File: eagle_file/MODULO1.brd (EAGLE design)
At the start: 160 x 100 mm, 6 parts, among them IC1 MCP23017SP

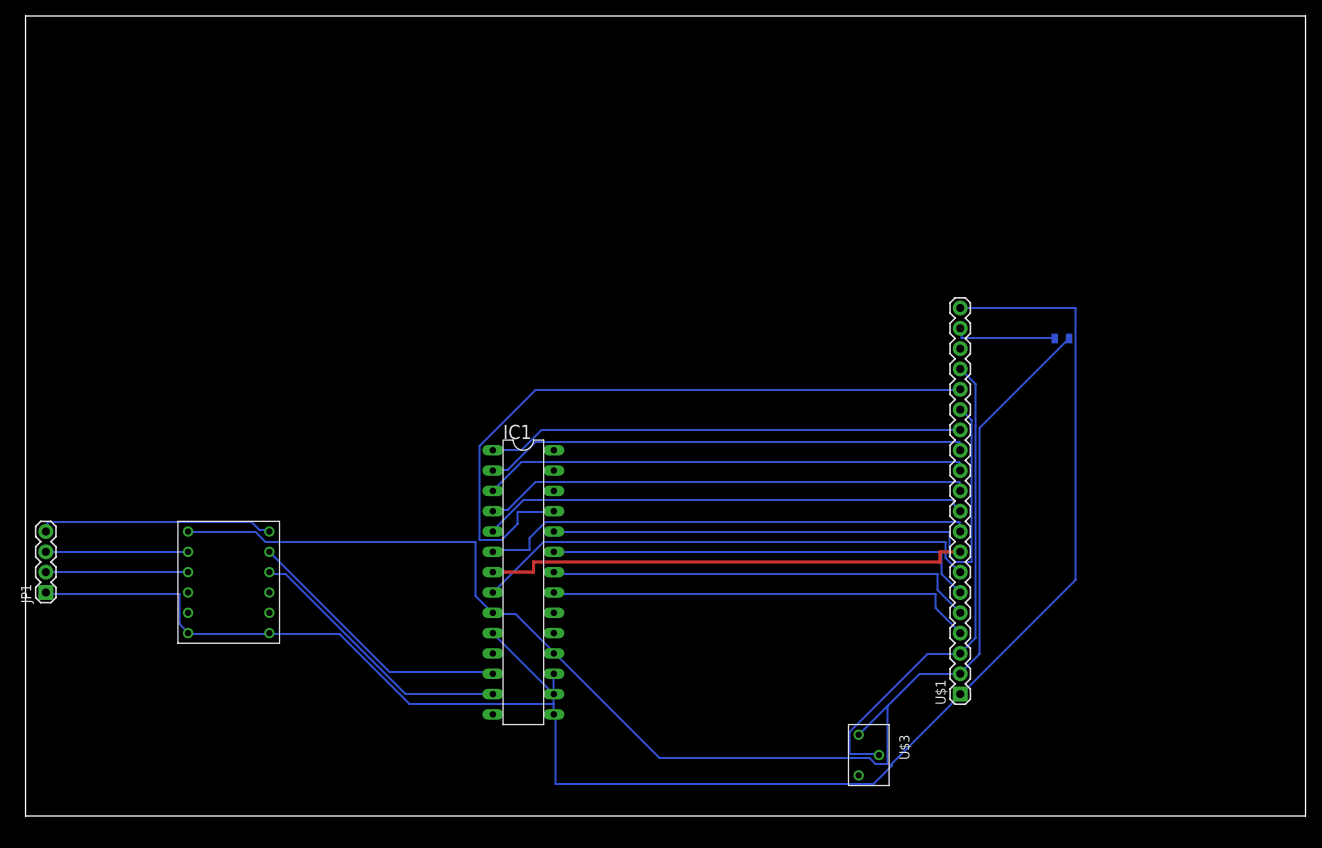
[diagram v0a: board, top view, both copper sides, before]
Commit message: Modulo 0 pdf
Modulo 0 senza contorno ai fori
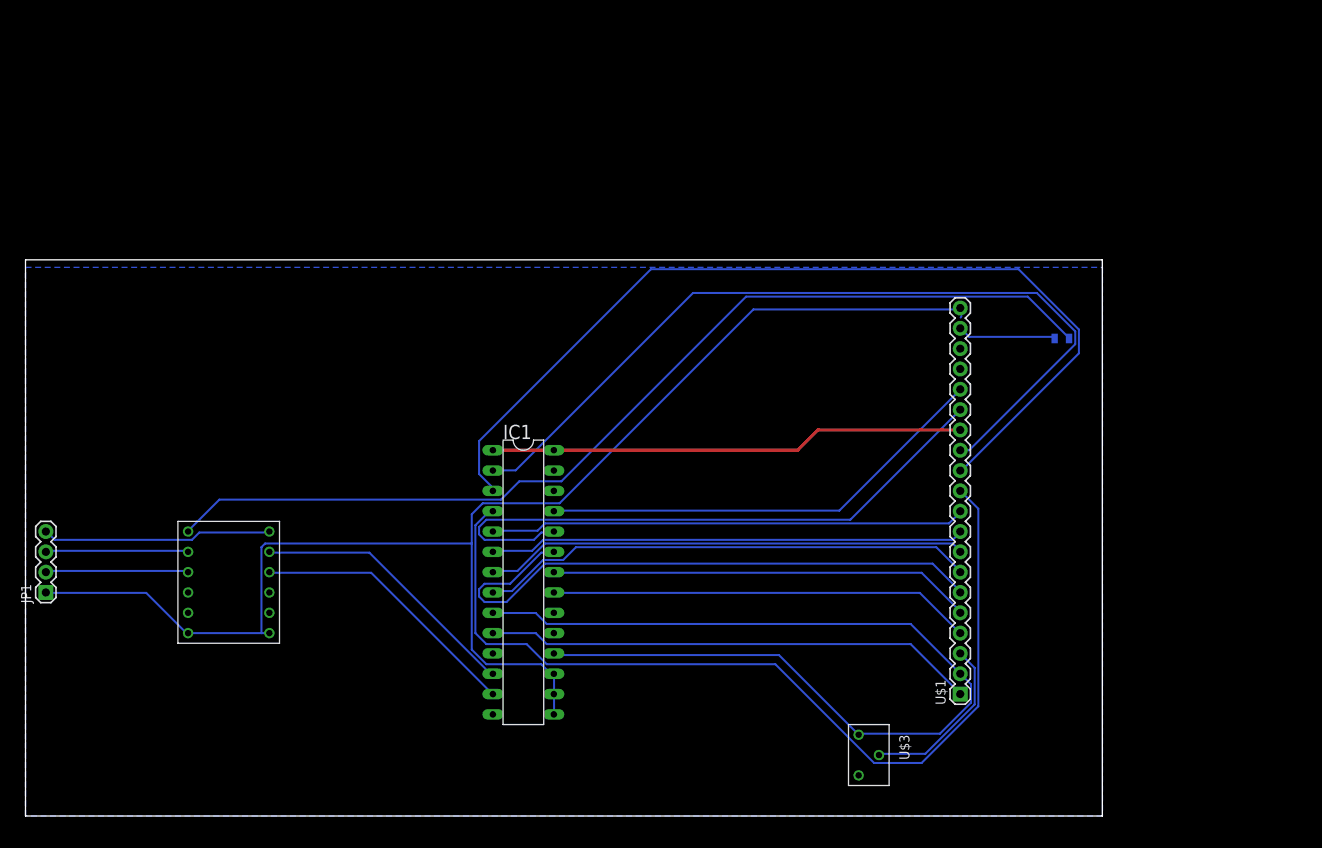
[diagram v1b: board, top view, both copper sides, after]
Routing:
- net N$14: track 174.1 -> 248.4 mm
- net N$8: track 60.9 -> 117.8 mm
- net N$9: track 61.0 -> 116.8 mm
- net N$7: track 60.9 -> 105.4 mm
- net N$21: track 61.5 -> 21.7 mm
- net N$5: track 86.5 -> 57.2 mm
- net N$3: track 54.5 -> 76.2 mm
- net GND: track 220.4 -> 234.6 mm
- net N$11: track 62.0 -> 59.5 mm
- net N$4: track 75.2 -> 77.2 mm
- net N$13: track 63.8 -> 62.2 mm
- net N$10: track 61.0 -> 59.5 mm
- net N$2: track 54.1 -> 53.0 mm
- net N$1: track 53.9 -> 52.9 mm
- net N$17: track 29.5 -> 28.8 mm
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- added copper zone on layer 16, net GND
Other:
- board size 160 x 100 mm -> 134.6 x 69.5 mm

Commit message: Modulo 2_1
Modolo2_1.pdf per controllare i footprint
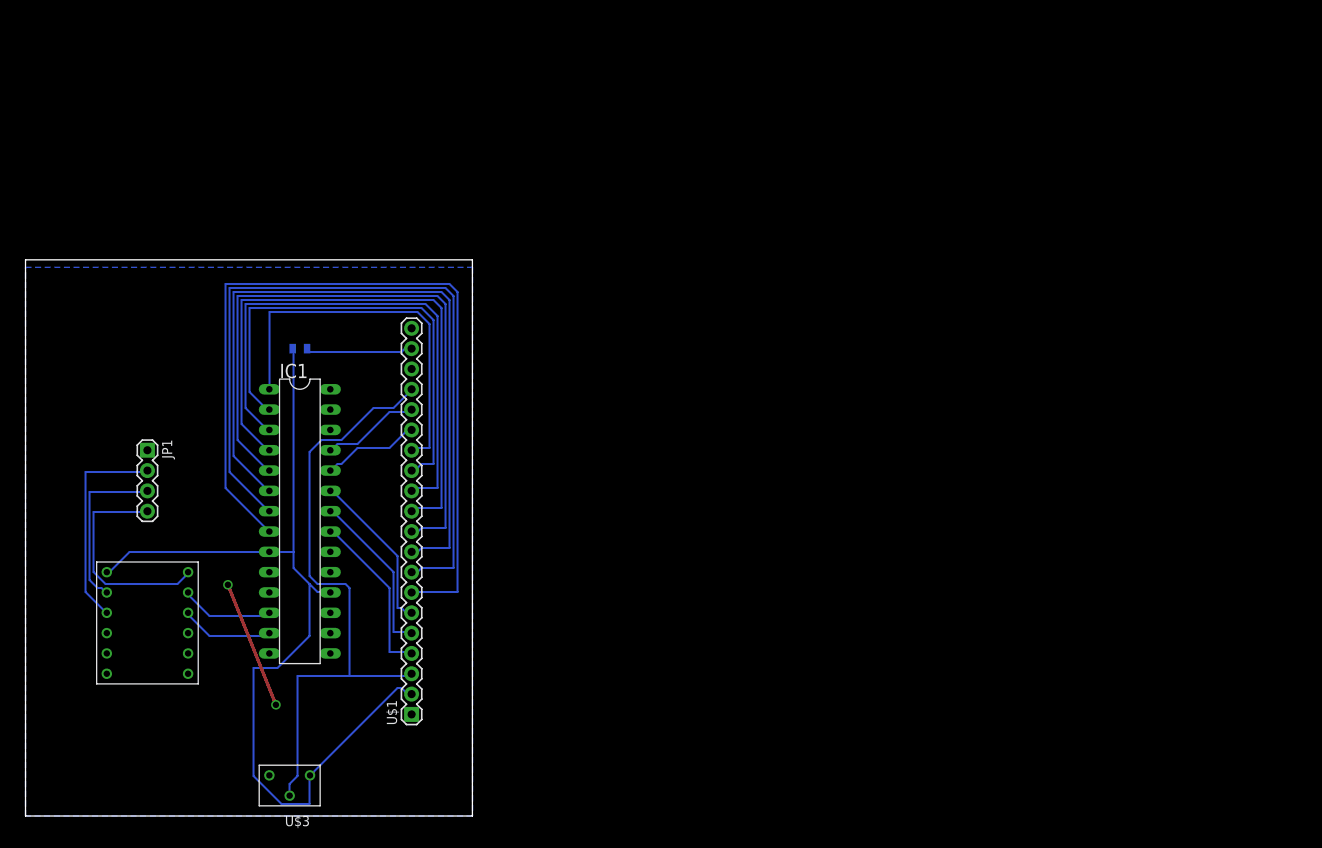
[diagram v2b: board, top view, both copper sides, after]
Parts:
- moved R1 95.3 mm to (34.3, 58.4), turned to 0 degrees
- moved U$3 71.2 mm to (33.0, 5.08), turned to 180 degrees
- moved U$1 68.6 mm to (48.3, 12.7)
- moved IC1 29.0 mm to (34.3, 36.8)
- moved JP1 21.8 mm to (15.2, 45.7), turned to 270 degrees
- moved U$2 11.4 mm to (15.2, 24.1)
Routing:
- net GND: track 234.6 -> 16.2 mm, vias 0 -> 2
- net N$14: track 248.4 -> 115.9 mm
- net N$4: track 77.2 -> 12.2 mm
- net N$21: track 21.7 -> 77.9 mm
- net N$3: track 76.2 -> 20.2 mm
- net N$8: track 117.8 -> 66.6 mm
- net N$7: track 105.4 -> 58.6 mm
- net N$5: track 57.2 -> 12.2 mm
- net N$13: track 62.2 -> 105.9 mm
- net N$9: track 116.8 -> 74.7 mm
- net N$12: track 60.4 -> 97.9 mm
- net N$2: track 53.0 -> 20.8 mm
- net N$1: track 52.9 -> 21.1 mm
- net N$11: track 59.5 -> 90.1 mm
- net N$10: track 59.5 -> 82.4 mm
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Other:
- board size 134.6 x 69.5 mm -> 55.9 x 69.5 mm
